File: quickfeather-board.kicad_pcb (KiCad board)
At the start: 4 copper layers, 58.4 x 22.9 mm, 100 parts, among them IC1 EOS-S3-QFN, J1 61300211121, J2 1x12_pinhead, J3 1x16_pinhead, J4 S2B-PH-SM4-TB_LF__SN_, J5 0473460001, J6 FTSH-105-01-L-DV-K, J7 61300211121, J8 2x8_pinhead, M1 mounting_pad, M2 mounting_pad, M3 mounting_pad, M4 mounting_pad, Q1 NX3008CBKV, Q2 2N7002PV, Q3 2N7002PV, Q4 DMG1012T-7, U1 TPS62821DLCR, U2 MCP73831T-2ACI_OT, U3 GD25Q16CWIGR, U4 DPS310, U5 MC3635, X1 ECS-_327-12_5-34B-TR

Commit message: Add release 1.2.0
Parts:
- added R27: R_1k5_0402, quickfeather-board-footprints:0402-res, F.Cu at (149.8, 113.1)
- moved R28 3.05 mm to (151.6, 112.7), turned to 270 degrees
- moved R29 3.02 mm to (153.5, 112.7), turned to 270 degrees
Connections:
- net /S3IO_27 renamed /S3IO_30
- net Net-(IC1-Pad18) renamed /S3IO_35_SPI_MST_CS3
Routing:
- net Net-(J3-Pad11): track 6.76 -> 10.3 mm
- net /ADC1: track 17.6 -> 21.0 mm
- net Net-(J3-Pad10): track 6.60 -> 9.87 mm
- net /PU_CTRL_USBP: track 1.81 -> 4.53 mm
- net /S3IO_40: track 31.9 -> 29.2 mm
- net /S3IO_30: track 12.8 -> 10.3 mm
- net /USB_D_P: track 34.6 -> 35.9 mm, vias 3 -> 2
- net /USB_D_N: track 29.9 -> 29.4 mm
- net Net-(J3-Pad7): track 6.51 -> 5.98 mm
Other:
- board text added: "J2"
- board text added: "J3"
- board text added: "J8"
- board text added: "QuickFeather 1.2"
- board text added: "Release 1.2.0"
- board text removed: "Prototype"
- board text removed: "QuickFeather 1.1"
- board text removed: "Rev. 1.1"

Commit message: Add release 1.2.1
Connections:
- IC1 pad 13: /S3IO_40 -> /PU_CTRL_USBN
- R27 pad 1: /PU_CTRL_USBP -> /PU_CTRL_USBN
- R42 pad 11: /J8.14 -> Net-(R42-Pad11)
- R42 pad 6: /S3IO_40 -> Net-(R42-Pad6)
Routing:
- net /S3IO_40: track 29.2 -> 0.00 mm, vias 3 -> 0
- net /J8.14: track 10.1 -> 0.00 mm
- net /PU_CTRL_USBN: track 0.00 -> 4.74 mm, vias 0 -> 2
- net /PU_CTRL_USBP: track 4.53 -> 1.81 mm
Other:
- board text added: "IO_29 IO_24 IO_11 IO_4 IO_8 NC"
- board text added: "PDM_CKO I2S_DOUT S3IO_11 S3IO_4 USR_BUTTON S3IO_8 NC GND"
- board text added: "Release 1.2.1"
- board text removed: "IO_29 IO_24 IO_11 IO_4 IO_8 IO_40"
- board text removed: "PDM_CKO I2S_DOUT S3IO_11 S3IO_4 USR_BUTTON S3IO_8 S3IO_40 GND"
- board text removed: "Release 1.2.0"

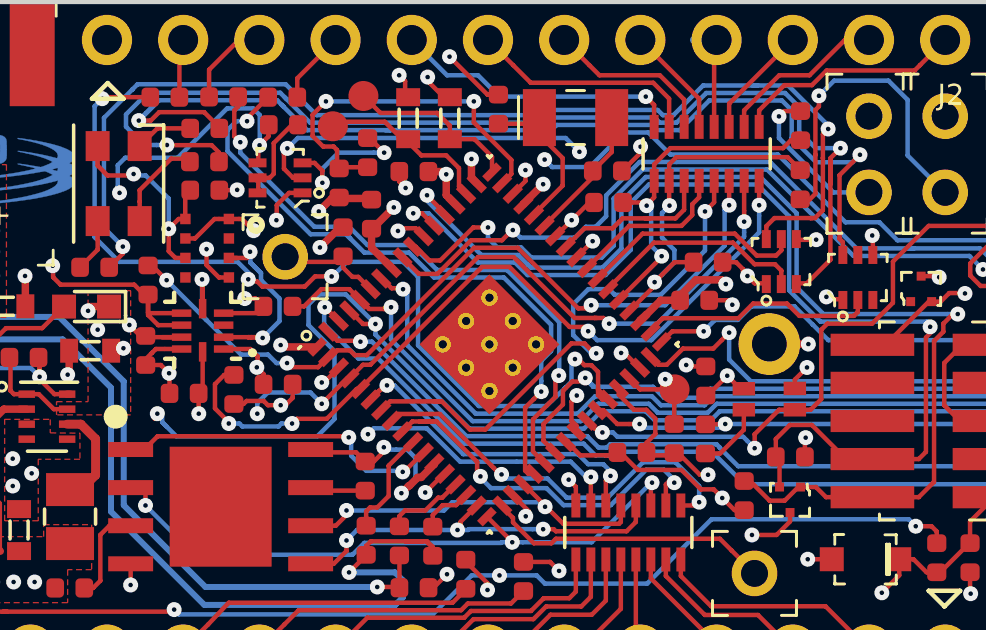
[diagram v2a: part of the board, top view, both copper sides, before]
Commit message: Update IM69D130 and PG-VLGA-8-2
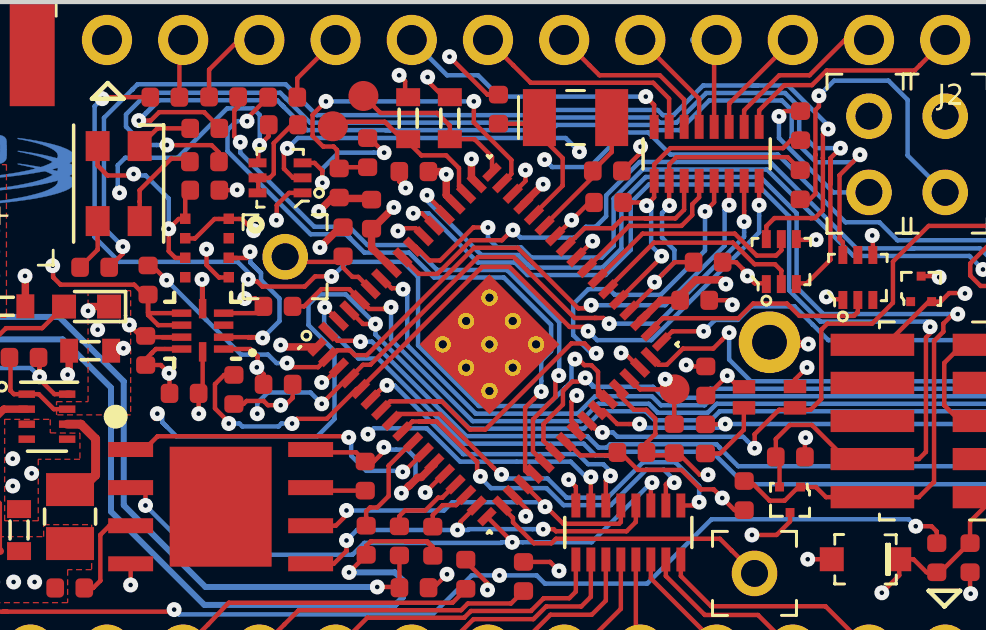
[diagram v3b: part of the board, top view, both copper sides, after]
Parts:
- moved MIC1 0.06 mm to (161.7, 104.9)
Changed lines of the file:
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@@
   (layers
     (0 Top signal)
-    (1 In1.Cu signal)
-    (2 In2.Cu mixed)
-    (31 Bottom signal)
+    (1 In1.Cu signal hide)
+    (2 In2.Cu mixed hide)
+    (31 Bottom signal hide)
     (32 B.Adhes user hide)
     (33 F.Adhes user hide)
@@
     (42 Eco1.User user hide)
     (43 Eco2.User user hide)
-    (44 Edge.Cuts user hide)
+    (44 Edge.Cuts user)
     (45 Margin user hide)
     (46 B.CrtYd user hide)
@@
     (add_net +VBUS)
   )
-  (module quickfeather-board-footprints:0402-res (layer Top)
-    (at 149.8453 113.1017 180)
-    (descr "Resistor SMD 0402 (1005 Metric), square (rectangular) end terminal, IPC_7351 nominal, (Body size source: http://www.tortai-tech.com/upload/download/2011102023233369053.pdf), generated with kicad-footprint-generator")
-    (tags resistor)
+  (module quickfeather-board-footprints:IM69D130 (layer Top)
+    (at 161.6953 104.9267)
     (attr smd)
-    (fp_text reference R27 (at 0 -1.17) (layer F.SilkS) hide
+    (fp_text reference MIC1 (at 0.41 -3.29) (layer F.SilkS) hide
       (effects (font (size 1 1) (thickness 0.15)))
     )
-    (fp_text value R_1k5_0402 (at 0 1.17) (layer F.Fab)
+    (fp_text value IM69D130 (at 1.95 -2.01) (layer F.Fab) hide
       (effects (font (size 1 1) (thickness 0.15)))
     )
-    (fp_text user %R (at 0 0) (layer F.Fab)
-      (effects (font (size 0.25 0.25) (thickness 0.04)))
-    )
-    (fp_line (start 0.93 0.47) (end -0.93 0.47) (layer F.CrtYd) (width 0.05))
-    (fp_line (start 0.93 -0.47) (end 0.93 0.47) (layer F.CrtYd) (width 0.05))
-    (fp_line (start -0.93 -0.47) (end 0.93 -0.47) (layer F.CrtYd) (width 0.05))
-    (fp_line (start -0.93 0.47) (end -0.93 -0.47) (layer F.CrtYd) (width 0.05))
-    (fp_line (start 0.5 0.25) (end -0.5 0.25) (layer F.Fab) (width 0.1))
-    (fp_line (start 0.5 -0.25) (end 0.5 0.25) (layer F.Fab) (width 0.1))
-    (fp_line (start -0.5 -0.25) (end 0.5 -0.25) (layer F.Fab) (width 0.1))
-    (fp_line (start -0.5 0.25) (end -0.5 -0.25) (layer F.Fab) (width 0.1))
-    (pad 2 smd roundrect (at 0.485 0 180) (size 0.59 0.64) (layers Top F.Paste F.Mask) (roundrect_rratio 0.25)
-      (net 3 /USB_D_N))
-    (pad 1 smd roundrect (at -0.485 0 180) (size 0.59 0.64) (layers Top F.Paste F.Mask) (roundrect_rratio 0.25)
-      (net 136 /PU_CTRL_USBN))
-    (model ${KIPRJMOD}/lib/3d-models/0402-res.step
-      (offset (xyz 0 0 -0.01))
+    (fp_line (start -0.762 2.794) (end -1.524 1.778) (layer F.Fab) (width 0.12))
+    (fp_line (start -1.524 2.794) (end -1.524 -1.27) (layer F.Fab) (width 0.12))
+    (fp_line (start 1.524 2.794) (end -1.524 2.794) (layer F.Fab) (width 0.12))
+    (fp_line (start 1.524 -1.27) (end 1.524 2.794) (layer F.Fab) (width 0.12))
+    (fp_line (start -1.524 -1.27) (end 1.524 -1.27) (layer F.Fab) (width 0.12))
+    (fp_line (start -0.8 2.71) (end -1.5 2.71) (layer F.CrtYd) (width 0.15))
+    (fp_line (start -0.8 2.71) (end 1.5 2.71) (layer F.CrtYd) (width 0.15))
+    (fp_line (start -1.5 -1.32) (end 0.01 -1.32) (layer F.CrtYd) (width 0.15))
+    (fp_line (start -1.5 2.71) (end -1.5 -1.32) (layer F.CrtYd) (width 0.15))
+    (fp_line (start 1.5 -1.32) (end 1.5 2.71) (layer F.CrtYd) (width 0.15))
+    (fp_line (start 0 -1.32) (end 1.5 -1.32) (layer F.CrtYd) (width 0.15))
+    (fp_circle (center 0.005 -0.006) (end 0.005 -0.406) (layer Dwgs.User) (width 0.1))
+    (fp_circle (center 0.005 -0.006) (end 0.005 -0.586) (layer Dwgs.User) (width 0.1))
+    (pad 4 smd rect (at 0.85 1.47 90) (size 0.45 0.75) (layers Top F.Paste F.Mask)
+      (net 1 GND))
+    (pad 3 smd rect (at 0.85 2.18 90) (size 0.45 0.75) (layers Top F.Paste F.Mask)
+      (net 105 /PDM_CKO))
+    (pad 2 smd rect (at -0.85 1.48 90) (size 0.45 0.75) (layers Top F.Paste F.Mask)
+      (net 2 +3V3))
+    (pad 1 smd rect (at -0.85 2.18 90) (size 0.45 0.75) (layers Top F.Paste F.Mask)
+      (net 19 "Net-(MIC1-Pad1)"))
+    (pad 5 thru_hole circle (at 0 -0.01 90) (size 2.06 2.06) (drill 1.16) (layers *.Mask Top)
+      (net 1 GND))
+    (model ${KIPRJMOD}/lib/3d-models/IM69D130.step
+      (offset (xyz 0 -0.7 0))
       (scale (xyz 1 1 1))
-      (rotate (xyz 0 0 0))
+      (rotate (xyz 0 0 180))
     )
   )
   (module quickfeather-board-footprints:PG-VLGA-8-2 (layer Top)
-    (at 142.95 101.785)
-    (fp_text reference U4 (at 0.8 -0.05) (layer F.SilkS) hide
-      (effects (font (size 0.7 0.7) (thickness 0.15)))
+    (at 142.9453 101.7767)
+    (attr smd)
+    (fp_text reference U4 (at -3.5 1) (layer F.SilkS) hide
+      (effects (font (size 1 1) (thickness 0.15)))
     )
-    (fp_text value DPS310 (at -0.05 -0.55) (layer F.Fab) hide
+    (fp_text value DPS310 (at -1.32 -2.328) (layer F.Fab) hide
       (effects (font (size 1 1) (thickness 0.15)))
     )
@@
     )
   )
-  (module quickfeather-board-footprints:IM69D130 (layer Top)
-    (at 161.69 104.99)
-    (fp_text reference MIC1 (at -2.18 0.34 -270) (layer F.SilkS) hide
-      (effects (font (size 0.7 0.7) (thickness 0.15)))
+  (module quickfeather-board-footprints:0402-res (layer Top)
+    (at 149.8453 113.1017 180)
+    (descr "Resistor SMD 0402 (1005 Metric), square (rectangular) end terminal, IPC_7351 nominal, (Body size source: http://www.tortai-tech.com/upload/download/2011102023233369053.pdf), generated with kicad-footprint-generator")
+    (tags resistor)
+    (attr smd)
+    (fp_text reference R27 (at 0 -1.17) (layer F.SilkS) hide
+      (effects (font (size 1 1) (thickness 0.15)))
     )
-    (fp_text value IM69D130 (at 1.95 -2.01) (layer F.Fab) hide
+    (fp_text value R_1k5_0402 (at 0 1.17) (layer F.Fab)
       (effects (font (size 1 1) (thickness 0.15)))
     )
-    (fp_line (start -0.762 2.794) (end -1.524 1.778) (layer F.Fab) (width 0.12))
-    (fp_line (start -1.524 2.794) (end -1.524 -1.27) (layer F.Fab) (width 0.12))
-    (fp_line (start 1.524 2.794) (end -1.524 2.794) (layer F.Fab) (width 0.12))
-    (fp_line (start 1.524 -1.27) (end 1.524 2.794) (layer F.Fab) (width 0.12))
-    (fp_line (start -1.524 -1.27) (end 1.524 -1.27) (layer F.Fab) (width 0.12))
-    (fp_line (start -0.8 2.71) (end -1.5 2.71) (layer F.CrtYd) (width 0.15))
-    (fp_line (start -0.8 2.71) (end 1.5 2.71) (layer F.CrtYd) (width 0.15))
-    (fp_line (start -1.5 -1.32) (end 0.01 -1.32) (layer F.CrtYd) (width 0.15))
-    (fp_line (start -1.5 2.71) (end -1.5 -1.32) (layer F.CrtYd) (width 0.15))
-    (fp_line (start 1.5 -1.32) (end 1.5 2.71) (layer F.CrtYd) (width 0.15))
-    (fp_line (start 0 -1.32) (end 1.5 -1.32) (layer F.CrtYd) (width 0.15))
-    (fp_circle (center 0.005 -0.006) (end 0.005 -0.406) (layer Dwgs.User) (width 0.1))
-    (fp_circle (center 0.005 -0.006) (end 0.005 -0.586) (layer Dwgs.User) (width 0.1))
-    (pad 4 smd rect (at 0.85 1.47 90) (size 0.45 0.75) (layers Top F.Paste F.Mask)
-      (net 1 GND))
-    (pad 3 smd rect (at 0.85 2.18 90) (size 0.45 0.75) (layers Top F.Paste F.Mask)
-      (net 105 /PDM_CKO))
-    (pad 2 smd rect (at -0.85 1.48 90) (size 0.45 0.75) (layers Top F.Paste F.Mask)
-      (net 2 +3V3))
-    (pad 1 smd rect (at -0.85 2.18 90) (size 0.45 0.75) (layers Top F.Paste F.Mask)
-      (net 19 "Net-(MIC1-Pad1)"))
-    (pad 5 thru_hole circle (at 0 -0.01 90) (size 2.06 2.06) (drill 1.16) (layers *.Mask Top)
-      (net 1 GND))
-    (model ${KIPRJMOD}/lib/3d-models/IM69D130.step
-      (offset (xyz 0 -0.7 0))
+    (fp_text user %R (at 0 0) (layer F.Fab)
+      (effects (font (size 0.25 0.25) (thickness 0.04)))
+    )
+    (fp_line (start 0.93 0.47) (end -0.93 0.47) (layer F.CrtYd) (width 0.05))
+    (fp_line (start 0.93 -0.47) (end 0.93 0.47) (layer F.CrtYd) (width 0.05))
+    (fp_line (start -0.93 -0.47) (end 0.93 -0.47) (layer F.CrtYd) (width 0.05))
+    (fp_line (start -0.93 0.47) (end -0.93 -0.47) (layer F.CrtYd) (width 0.05))
+    (fp_line (start 0.5 0.25) (end -0.5 0.25) (layer F.Fab) (width 0.1))
+    (fp_line (start 0.5 -0.25) (end 0.5 0.25) (layer F.Fab) (width 0.1))
+    (fp_line (start -0.5 -0.25) (end 0.5 -0.25) (layer F.Fab) (width 0.1))
+    (fp_line (start -0.5 0.25) (end -0.5 -0.25) (layer F.Fab) (width 0.1))
+    (pad 2 smd roundrect (at 0.485 0 180) (size 0.59 0.64) (layers Top F.Paste F.Mask) (roundrect_rratio 0.25)
+      (net 3 /USB_D_N))
+    (pad 1 smd roundrect (at -0.485 0 180) (size 0.59 0.64) (layers Top F.Paste F.Mask) (roundrect_rratio 0.25)
+      (net 136 /PU_CTRL_USBN))
+    (model ${KIPRJMOD}/lib/3d-models/0402-res.step
+      (offset (xyz 0 0 -0.01))
       (scale (xyz 1 1 1))
-      (rotate (xyz 0 0 180))
+      (rotate (xyz 0 0 0))
     )
   )
@@
   (segment (start 151.582183 110.010458) (end 151.582183 110.017817) (width 0.15) (layer Top) (net 18))
   (segment (start 151.582183 110.017817) (end 151.25 110.35) (width 0.15) (layer Top) (net 18))
-  (via (at 150.2203 109.9267) (size 0.5) (drill 0.15) (layers Top Bottom) (net 136))
-  (segment (start 150.875076 109.303351) (end 150.843649 109.303351) (width 0.15) (layer Top) (net 136))
-  (segment (start 150.843649 109.303351) (end 150.2203 109.9267) (width 0.15) (layer Top) (net 136))
   (segment (start 160.84 107.545) (end 160.84 107.17) (width 0.15) (layer Top) (net 19))
   (segment (start 160.84 107.839002) (end 160.84 107.545) (width 0.15) (layer Top) (net 19))
@@
   (segment (start 153.144999 110.924001) (end 153.840998 111.62) (width 0.15) (layer Top) (net 135))
   (segment (start 153.840998 111.62) (end 154.425 111.62) (width 0.15) (layer Top) (net 135))
+  (via (at 150.2203 109.9267) (size 0.5) (drill 0.15) (layers Top Bottom) (net 136))
+  (segment (start 150.875076 109.303351) (end 150.843649 109.303351) (width 0.15) (layer Top) (net 136))
+  (segment (start 150.843649 109.303351) (end 150.2203 109.9267) (width 0.15) (layer Top) (net 136))
   (via (at 150.9453 112.6517) (size 0.5) (drill 0.15) (layers Top Bottom) (net 136))
   (segment (start 150.3303 113.1017) (end 150.4953 113.1017) (width 0.15) (layer Top) (net 136))

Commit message: Update docs for release 1.2.1
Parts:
- moved MIC1 0.06 mm to (161.7, 105.0)
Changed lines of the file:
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@@
   (layers
     (0 Top signal)
-    (1 In1.Cu signal hide)
-    (2 In2.Cu mixed hide)
-    (31 Bottom signal hide)
+    (1 In1.Cu signal)
+    (2 In2.Cu mixed)
+    (31 Bottom signal)
     (32 B.Adhes user hide)
     (33 F.Adhes user hide)
@@
     (42 Eco1.User user hide)
     (43 Eco2.User user hide)
-    (44 Edge.Cuts user)
+    (44 Edge.Cuts user hide)
     (45 Margin user hide)
     (46 B.CrtYd user hide)
@@
   )
   (module quickfeather-board-footprints:IM69D130 (layer Top)
-    (at 161.6953 104.9267)
+    (at 161.69 104.99)
     (attr smd)
-    (fp_text reference MIC1 (at 0.41 -3.29) (layer F.SilkS) hide
-      (effects (font (size 1 1) (thickness 0.15)))
+    (fp_text reference MIC1 (at -2.18 0.34 -270) (layer F.SilkS) hide
+      (effects (font (size 0.7 0.7) (thickness 0.15)))
     )
     (fp_text value IM69D130 (at 1.95 -2.01) (layer F.Fab) hide
@@
   )
   (module quickfeather-board-footprints:PG-VLGA-8-2 (layer Top)
-    (at 142.9453 101.7767)
+    (at 142.95 101.785)
     (attr smd)
-    (fp_text reference U4 (at -3.5 1) (layer F.SilkS) hide
+    (fp_text reference U4 (at 0.8 -0.05) (layer F.SilkS) hide
+      (effects (font (size 0.7 0.7) (thickness 0.15)))
+    )
+    (fp_text value DPS310 (at -0.05 -0.55) (layer F.Fab) hide
       (effects (font (size 1 1) (thickness 0.15)))
     )
-    (fp_text value DPS310 (at -1.32 -2.328) (layer F.Fab) hide
-      (effects (font (size 1 1) (thickness 0.15)))
-    )

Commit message: [#54927] Update to KiCad7
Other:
- net class Default removed
- net class Plane removed
